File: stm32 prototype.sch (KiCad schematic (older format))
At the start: 133 parts, among them J1 USB_B_Mini, J2 Conn_01x06, J3 Conn_01x02, J4 Conn_01x10, Q1 Q_NMOS_GSD, Q2 Q_NMOS_GSD, Q3 Q_NMOS_GSD, Q4 Q_NMOS_GSD, Q5 Q_NMOS_GSD, Q6 Q_NMOS_GSD, Q7 Q_NMOS_GSD, Q8 Q_NMOS_GSD, Q9 Q_NMOS_GSD, U1 FT232RL, U2 W25Q128JV-DTR, U3 STM32F407VGTx, U4 LD1117S33TR, U5 ESP32, U6 IS25LP016D-JNLE-TR, U7 TPS62203DBVR, Y1 Crystal_GND24, Y2 Crystal_GND23, Y3 Crystal_GND23

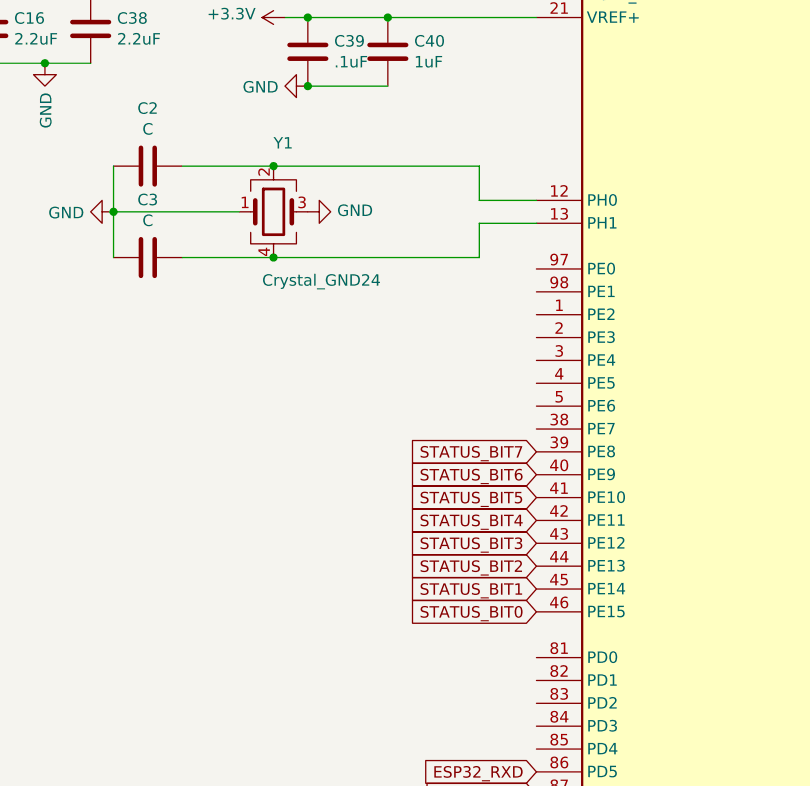
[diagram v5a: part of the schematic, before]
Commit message: laid out crystal oscilator, connected binary indicator leds
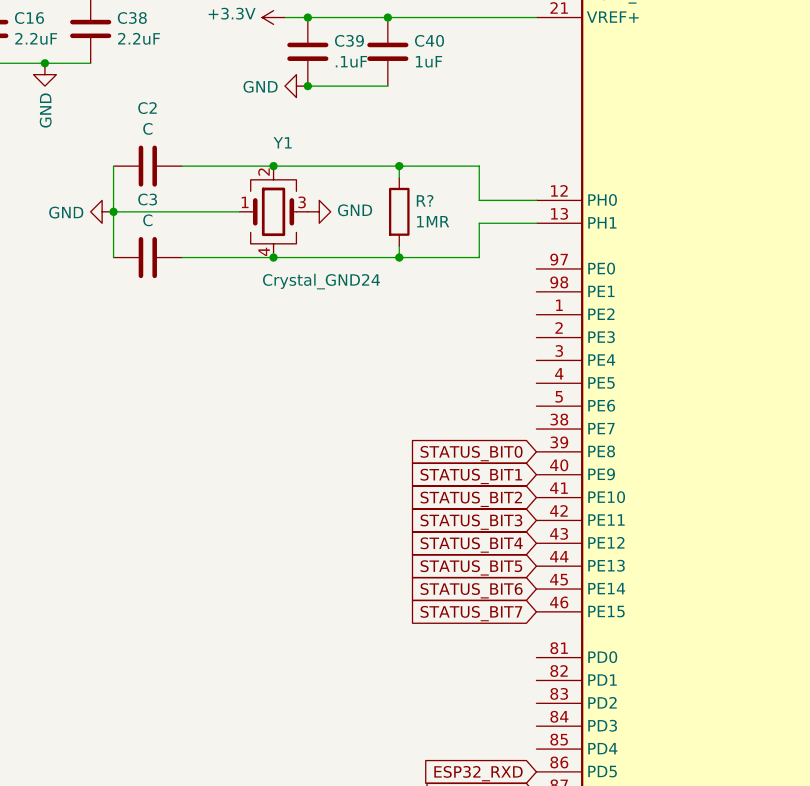
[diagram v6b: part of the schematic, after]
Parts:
- added R?: 1MR, Resistors_SMD:R_0603, symbol Device:R
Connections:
- net STATUS_BIT0: now also U3.39 (PE8); no longer U3.46 (PE15)
- net STATUS_BIT1: now also U3.40 (PE9); no longer U3.45 (PE14)
- net STATUS_BIT2: now also U3.41 (PE10); no longer U3.44 (PE13)
- net STATUS_BIT3: now also U3.42 (PE11); no longer U3.43 (PE12)
- net STATUS_BIT4: now also U3.43 (PE12); no longer U3.42 (PE11)
- net STATUS_BIT5: now also U3.44 (PE13); no longer U3.41 (PE10)
- net STATUS_BIT6: now also U3.45 (PE14); no longer U3.40 (PE9)
- net STATUS_BIT7: now also U3.46 (PE15); no longer U3.39 (PE8)
- net at C2.1, U3.12 (PH0), Y1.2: now also R?.1
- net at C3.1, U3.13 (PH1), Y1.4: now also R?.2
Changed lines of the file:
@@
 $EndComp
 Wire Wire Line
-	13300 6700 14200 6700
-Wire Wire Line
-	13300 7100 14200 7100
+	13300 6700 13850 6700
+Wire Wire Line
+	13300 7100 13850 7100
 Wire Wire Line
 	14200 7100 14200 6950
@@
 Text Notes 2200 6300 0    79   ~ 0
 POWER OK LEDS
+Text GLabel 14450 7950 0    50   Input ~ 0
+STATUS_BIT0
+Text GLabel 14450 8050 0    50   Input ~ 0
+STATUS_BIT1
+Text GLabel 14450 8150 0    50   Input ~ 0
+STATUS_BIT2
+Text GLabel 14450 8250 0    50   Input ~ 0
+STATUS_BIT3
+Text GLabel 14450 8350 0    50   Input ~ 0
+STATUS_BIT4
+Text GLabel 14450 8450 0    50   Input ~ 0
+STATUS_BIT5
+Text GLabel 14450 8550 0    50   Input ~ 0
+STATUS_BIT6
 Text GLabel 14450 8650 0    50   Input ~ 0
-STATUS_BIT0
-Text GLabel 14450 8550 0    50   Input ~ 0
-STATUS_BIT1
-Text GLabel 14450 8450 0    50   Input ~ 0
-STATUS_BIT2
-Text GLabel 14450 8350 0    50   Input ~ 0
-STATUS_BIT3
-Text GLabel 14450 8250 0    50   Input ~ 0
-STATUS_BIT4
-Text GLabel 14450 8150 0    50   Input ~ 0
-STATUS_BIT5
-Text GLabel 14450 8050 0    50   Input ~ 0
-STATUS_BIT6
-Text GLabel 14450 7950 0    50   Input ~ 0
 STATUS_BIT7
 $Comp
@@
 	8550 8800 8550 8700
 Connection ~ 8550 8700
+$Comp
+L Device:R R?
+U 1 1 5C048B74
+P 13850 6900
+F 0 "R?" H 13920 6946 50  0000 L CNN
+F 1 "1MR" H 13920 6855 50  0000 L CNN
+F 2 "Resistors_SMD:R_0603" V 13780 6900 50  0001 C CNN
+F 3 "~" H 13850 6900 50  0001 C CNN
+	1    13850 6900
+	1    0    0    -1
+$EndComp
+Wire Wire Line
+	13850 6750 13850 6700
+Connection ~ 13850 6700
+Wire Wire Line
+	13850 6700 14200 6700
+Wire Wire Line
+	13850 7050 13850 7100
+Connection ~ 13850 7100
+Wire Wire Line
+	13850 7100 14200 7100
 $EndSCHEMATC

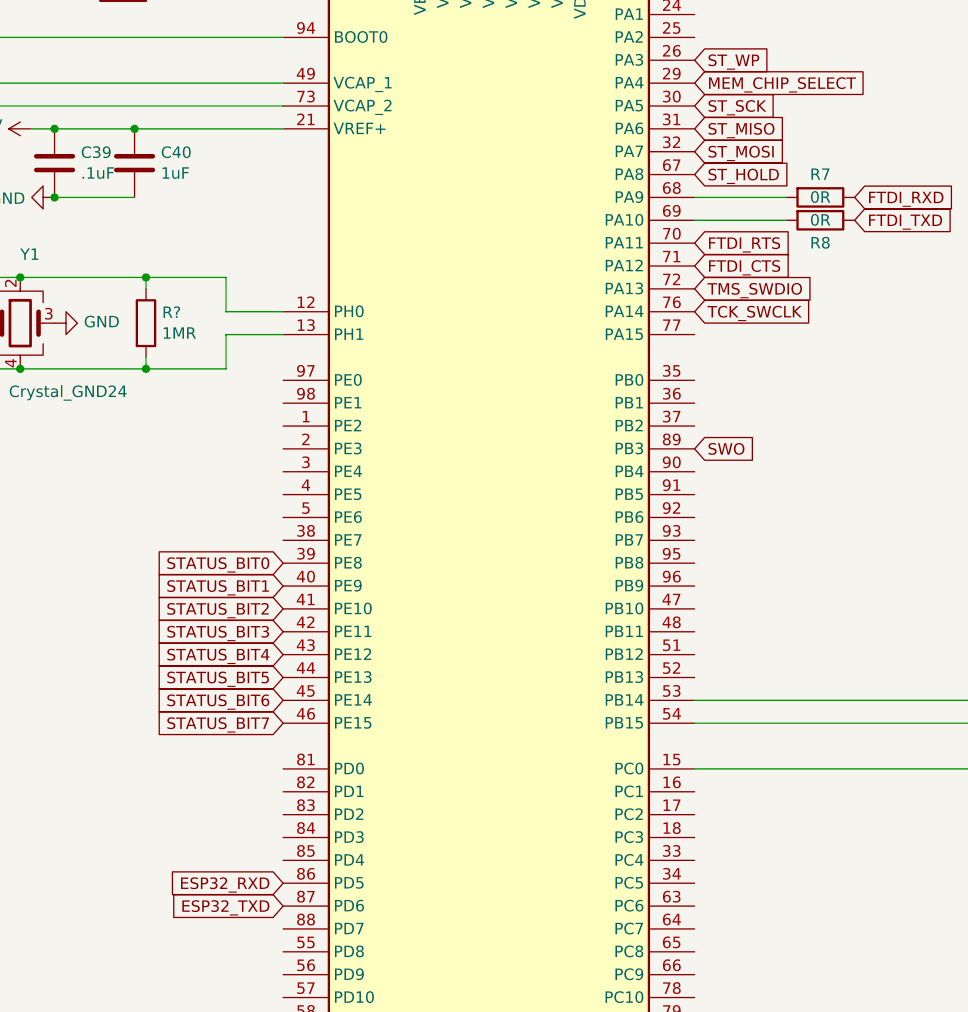
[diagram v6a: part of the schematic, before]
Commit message: worked on stm flash chip layout, stm bypass capacitor layout, changed antenna connection to sma
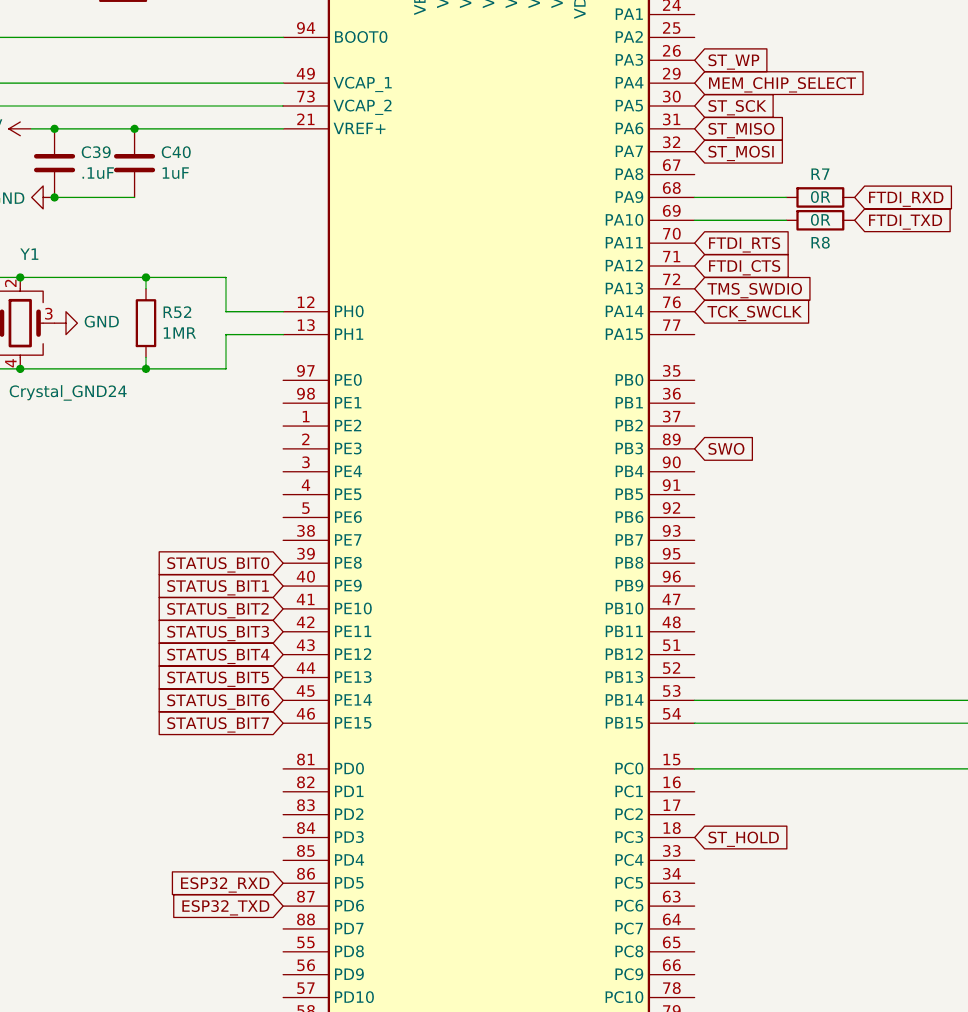
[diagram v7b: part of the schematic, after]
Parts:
- J3: footprint connectors_mdg:u.FL -> connectors_mdg:SMA_SMD_Jack_Straight
- gave numbers to parts that had none: 1
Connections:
- net ST_HOLD: now also U3.18 (PC3); no longer U3.67 (PA8)
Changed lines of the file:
@@
 F 0 "J3" H 29480 10492 50  0000 L CNN
 F 1 "Conn_01x02" H 29480 10401 50  0000 L CNN
-F 2 "connectors_mdg:u.FL" H 29400 10500 50  0001 C CNN
+F 2 "connectors_mdg:SMA_SMD_Jack_Straight" H 29400 10500 50  0001 C CNN
 F 3 "~" H 29400 10500 50  0001 C CNN
 F 4 "0734120110" H 29400 10500 50  0001 C CNN "Part Number"
@@
 Wire Wire Line
 	22800 5700 22950 5700
-Text GLabel 16250 6250 2    50   Input ~ 0
-ST_HOLD
 Text GLabel 16250 5750 2    50   Input ~ 0
 ST_WP
@@
 Connection ~ 8550 8700
 $Comp
-L Device:R R?
+L Device:R R52
 U 1 1 5C048B74
 P 13850 6900
-F 0 "R?" H 13920 6946 50  0000 L CNN
+F 0 "R52" H 13920 6946 50  0000 L CNN
 F 1 "1MR" H 13920 6855 50  0000 L CNN
 F 2 "Resistors_SMD:R_0603" V 13780 6900 50  0001 C CNN
@@
 Wire Wire Line
 	13850 7100 14200 7100
+Text GLabel 16250 9150 2    50   Input ~ 0
+ST_HOLD
 $EndSCHEMATC

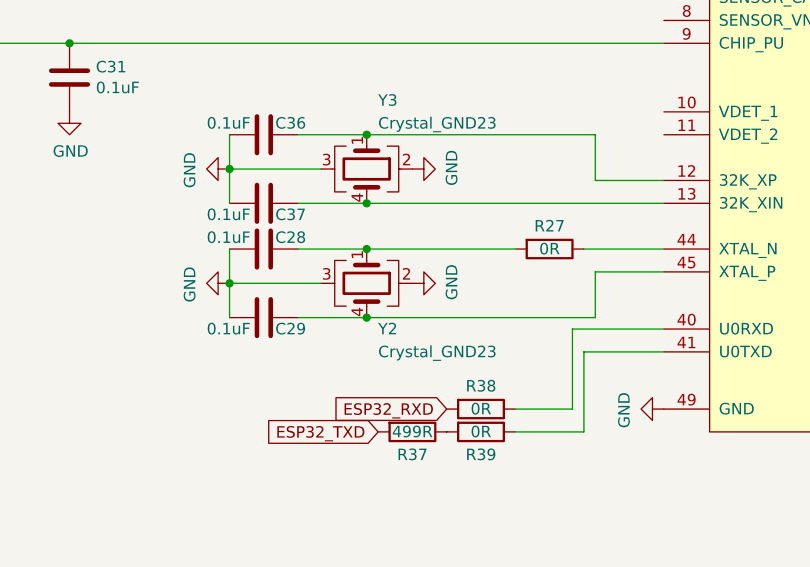
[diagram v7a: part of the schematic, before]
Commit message: did a little layout around esp32, need to check pinout of stm crystal, need to check trace width and spacing for esp32
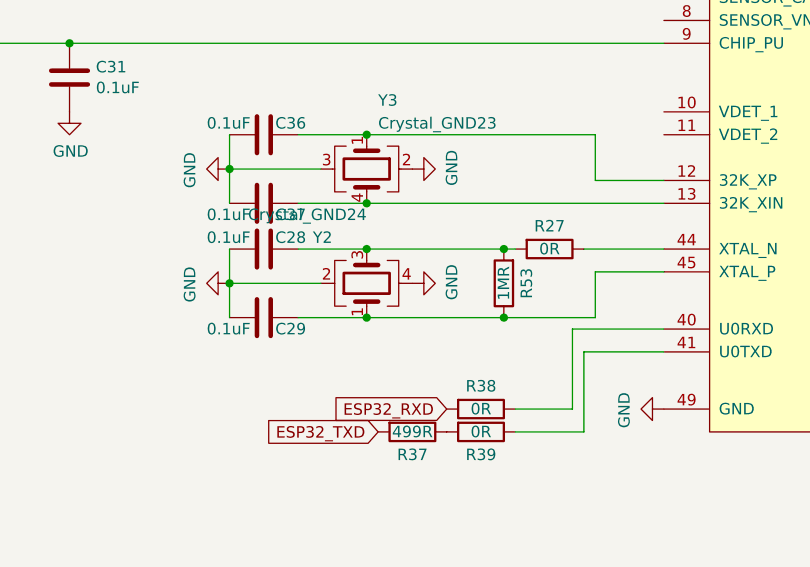
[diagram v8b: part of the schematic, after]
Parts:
- removed Y2: Crystal_GND23, Crystals:Crystal_SMD_SeikoEpson_TSX3225-4pin_3.2x2.5mm, symbol Device:Crystal_GND23
- added R53: 1MR, Resistors_SMD:R_0603, symbol Device:R
- added Y2: Crystal_GND24, Crystals:Crystal_SMD_SeikoEpson_TSX3225-4pin_3.2x2.5mm, symbol Device:Crystal_GND24
- J3: Part Number 0734120110 -> (none); Part Number - uFL (none) -> 0734120110; Part Number SMA (none) -> 0732511350
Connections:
- net GND: now also Y2.2, Y2.4
- net at C29.1, U5.45 (XTAL_P): now also R53.1, Y2.1
- net at C28.1, R27.2: now also R53.2, Y2.3
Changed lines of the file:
@@
-$EndComp
-$Comp
-L Device:Crystal_GND23 Y2
-U 1 1 5BECCC18
-P 25300 12950
-F 0 "Y2" V 25500 13000 50  0000 L CNN
-F 1 "Crystal_GND23" V 25600 13000 50  0000 L CNN
-F 2 "Crystals:Crystal_SMD_SeikoEpson_TSX3225-4pin_3.2x2.5mm" H 25300 12950 50  0001 C CNN
-F 3 "~" H 25300 12950 50  0001 C CNN
-	1    25300 12950
-	0    1    1    0
 $EndComp
 $Comp
@@
 $EndComp
 Wire Wire Line
-	25300 12800 25950 12800
-Wire Wire Line
 	26250 12800 26600 12800
 Wire Wire Line
@@
 	26300 12900 26300 13100
 Wire Wire Line
-	26300 13100 25300 13100
+	26300 13100 25900 13100
 $Comp
 L Device:C C28
@@
 	0    1    1    0
 $EndComp
-Wire Wire Line
-	25300 13100 25000 13100
-Connection ~ 25300 13100
-Wire Wire Line
-	25000 12800 25300 12800
-Connection ~ 25300 12800
 Wire Wire Line
 	24700 12800 24700 12950
@@
 F 2 "connectors_mdg:SMA_SMD_Jack_Straight" H 29400 10500 50  0001 C CNN
 F 3 "~" H 29400 10500 50  0001 C CNN
-F 4 "0734120110" H 29400 10500 50  0001 C CNN "Part Number"
+F 4 "0734120110" H 29400 10500 50  0001 C CNN "Part Number - uFL"
+F 5 " 0732511350 " H 29400 10500 50  0001 C CNN "Part Number SMA"
 	1    29400 10500
 	1    0    0    -1
@@
 Text GLabel 16250 9150 2    50   Input ~ 0
 ST_HOLD
+$Comp
+L Device:R R53
+U 1 1 5C09C464
+P 25900 12950
+F 0 "R53" V 25800 12950 50  0000 C CNN
+F 1 "1MR" V 25900 12950 50  0000 C CNN
+F 2 "Resistors_SMD:R_0603" V 25830 12950 50  0001 C CNN
+F 3 "~" H 25900 12950 50  0001 C CNN
+	1    25900 12950
+	-1   0    0    1
+$EndComp
+Connection ~ 25900 13100
+Connection ~ 25900 12800
+Wire Wire Line
+	25900 12800 25950 12800
+$Comp
+L Device:Crystal_GND24 Y2
+U 1 1 5C0A609D
+P 25300 12950
+F 0 "Y2" V 25500 13100 50  0000 L CNN
+F 1 "Crystal_GND24" V 25600 12950 50  0000 L CNN
+F 2 "Crystals:Crystal_SMD_SeikoEpson_TSX3225-4pin_3.2x2.5mm" H 25300 12950 50  0001 C CNN
+F 3 "~" H 25300 12950 50  0001 C CNN
+F 4 " FA-20H 40.0000MF10Z-K3 " V 25300 12950 50  0001 C CNN "Part Number"
+	1    25300 12950
+	0    -1   -1   0
+$EndComp
+Wire Wire Line
+	25000 12800 25300 12800
+Wire Wire Line
+	25000 13100 25300 13100
+Connection ~ 25300 13100
+Wire Wire Line
+	25300 13100 25900 13100
+Connection ~ 25300 12800
+Wire Wire Line
+	25300 12800 25900 12800
 $EndSCHEMATC
